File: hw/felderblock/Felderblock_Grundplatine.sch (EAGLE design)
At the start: 50 parts, among them IC1 LM311N, IC2 MC78M05CT, J1 RJ11, J2 RJ11, M1 ARDUINO-NANO-3.0, T2 BC337, X1 TASTENSPERRE1, X2 TASTENSPERRE2, X3 SCHL-SPERRE, X5 ANSCHALTER

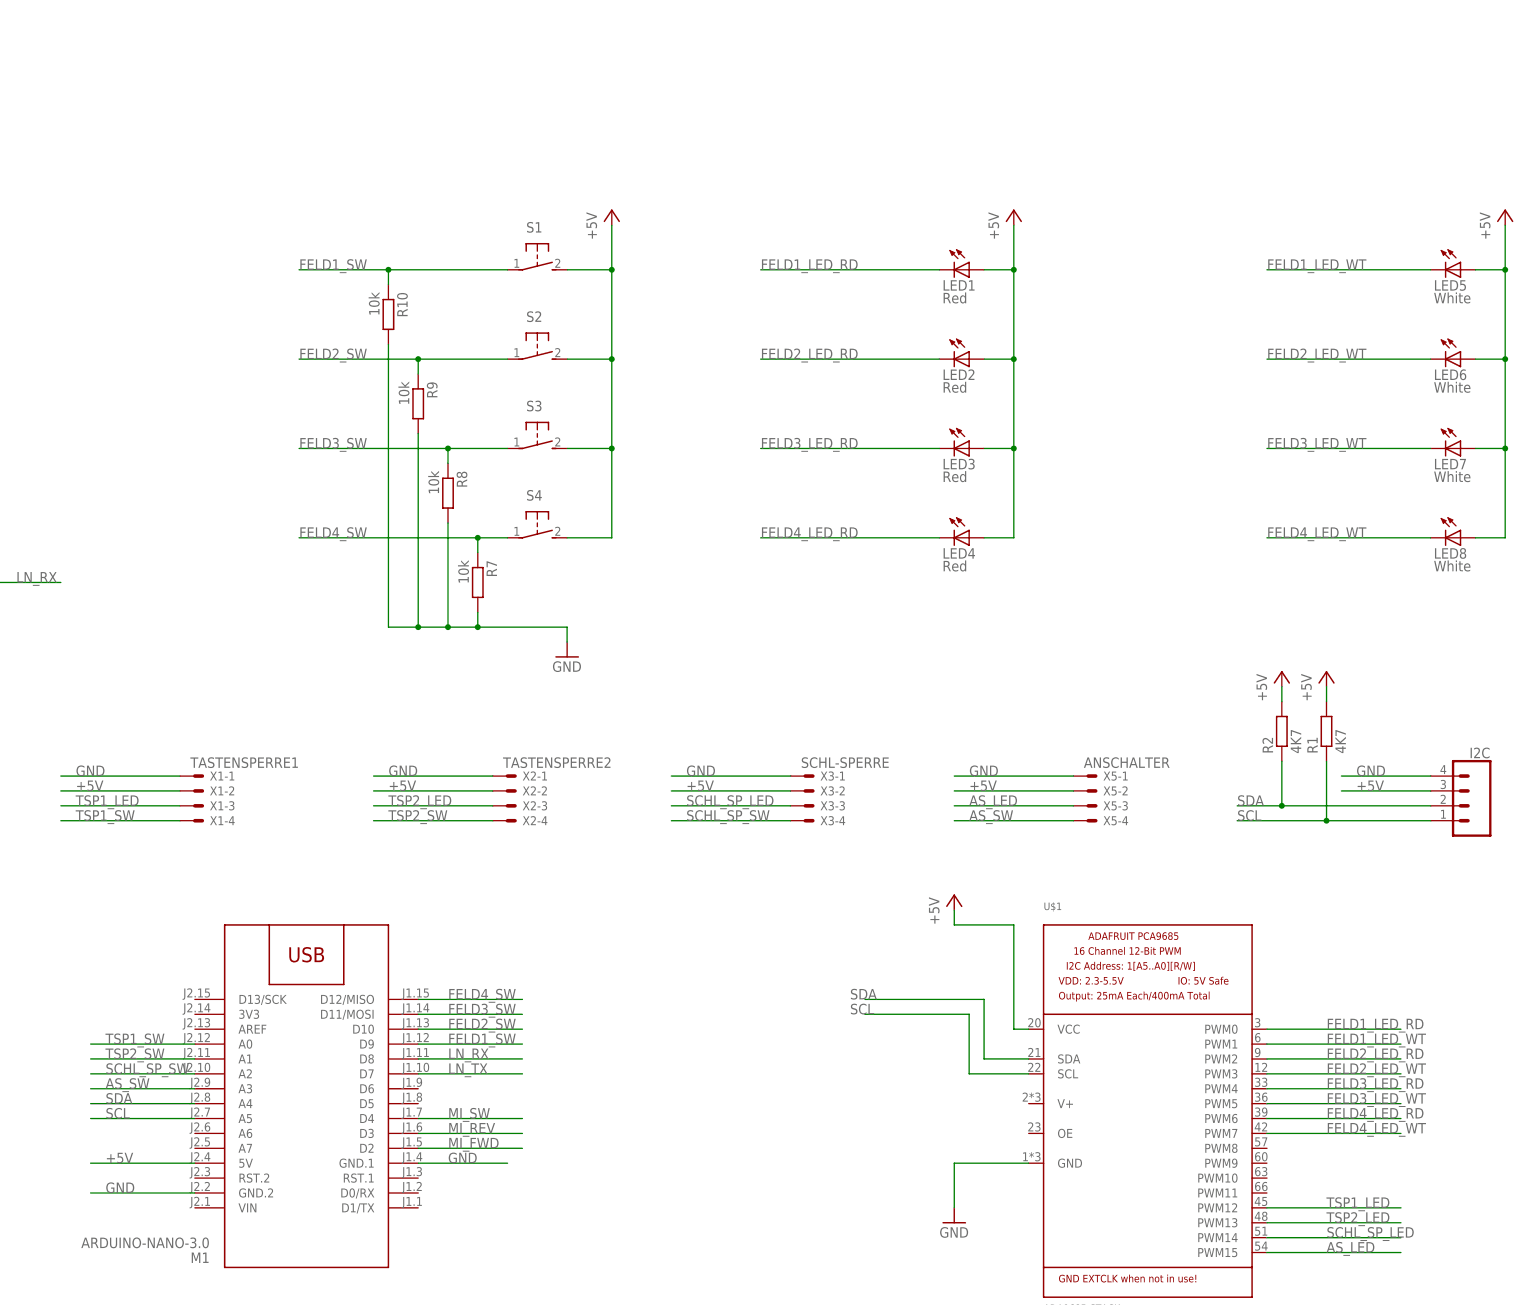
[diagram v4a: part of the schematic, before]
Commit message: Extended to six fields
Extended to six fields per PCB
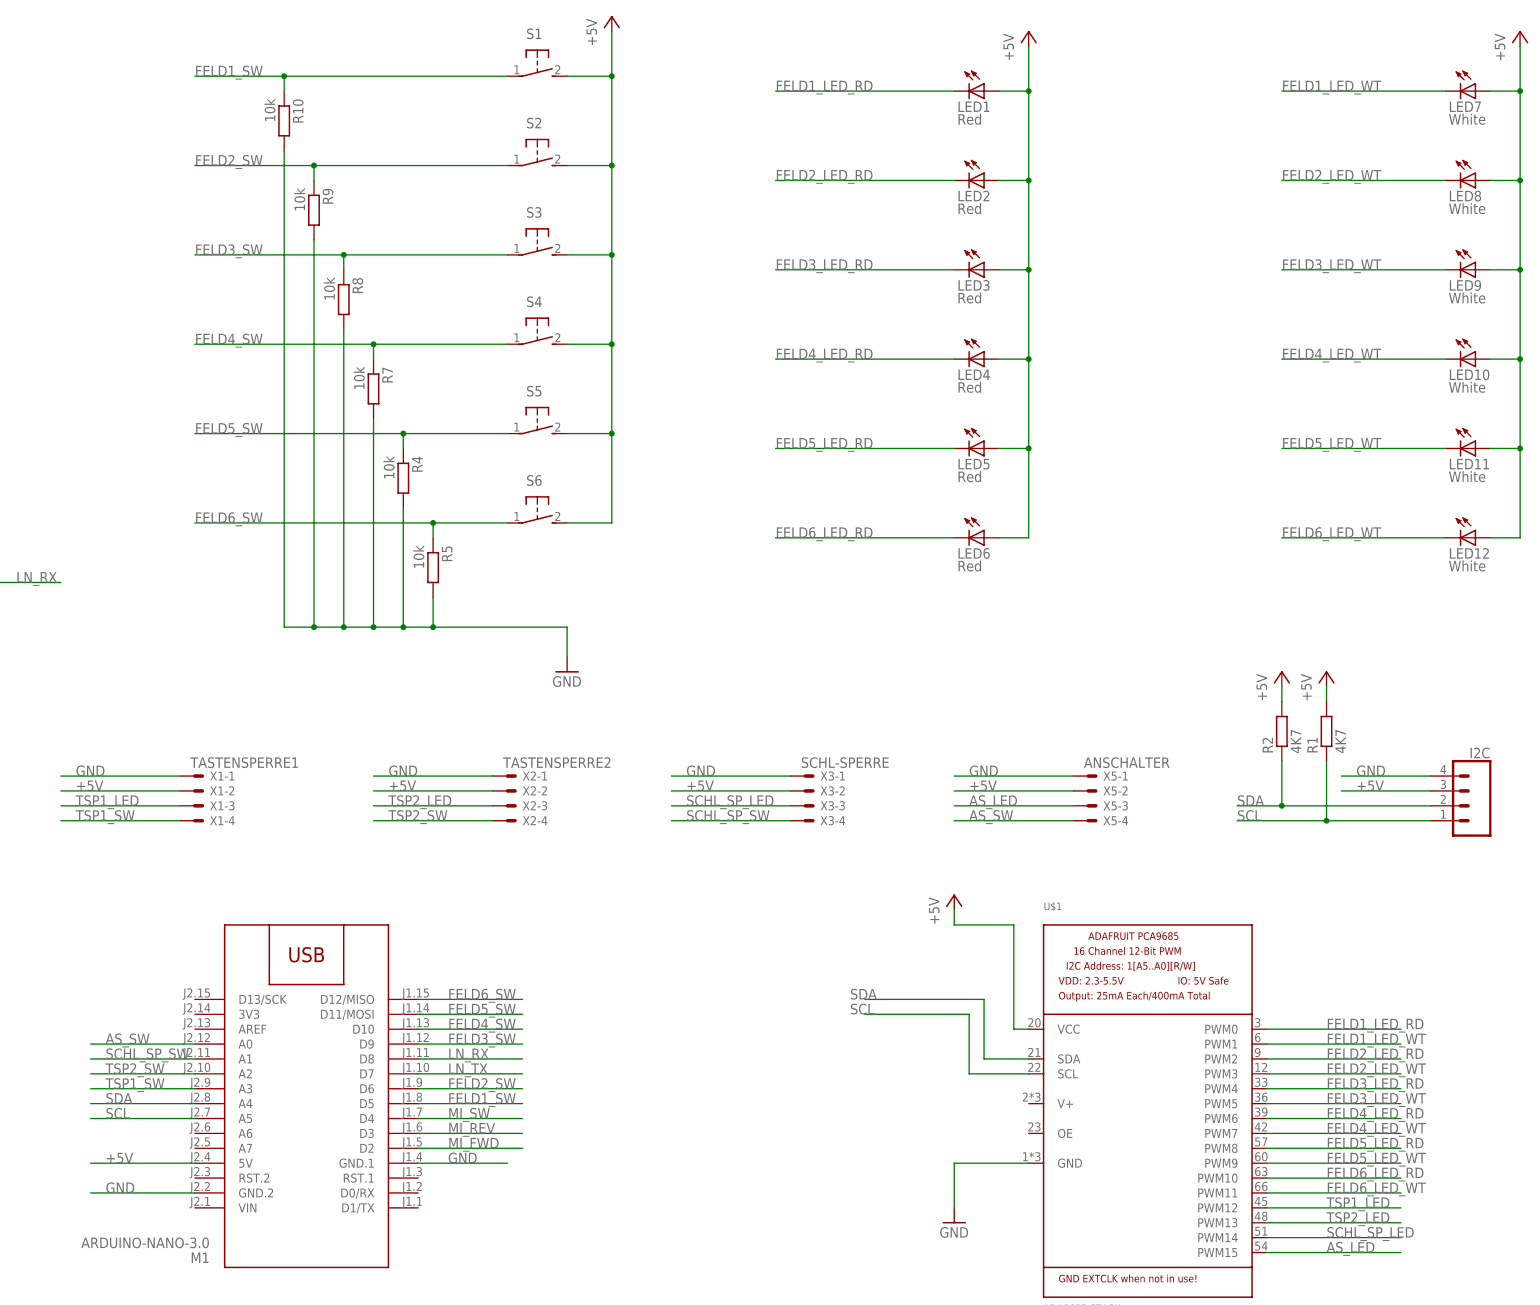
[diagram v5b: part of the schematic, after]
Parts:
- added LED10, LED11, LED12, LED9: White, led:LED3MM
- added R4, R5: 10k, resistor:R-EU_0207/7
- added S5, S6: (no value), adafruit:31-XX
- LED5, LED6: value White -> Red
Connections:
- new net FELD5_LED_RD: LED5.C, U$1.PWM8
- new net FELD5_LED_WT: LED11.C, U$1.PWM9
- new net FELD5_SW: M1.D11/MOSI, R4.1, S5.P
- new net FELD6_LED_RD: LED6.C, U$1.PWM10
- new net FELD6_LED_WT: LED12.C, U$1.PWM11
- new net FELD6_SW: M1.D12/MISO, R5.1, S6.P
- net +5V: now also LED10.A, LED11.A, LED12.A, LED9.A, S5.S, S6.S
- net AS_SW: now also M1.A0; no longer M1.A3
- net FELD1_LED_WT: now also LED7.C; no longer LED5.C
- net FELD1_SW: now also M1.D5; no longer M1.D9
- net FELD2_LED_WT: now also LED8.C; no longer LED6.C
- net FELD2_SW: now also M1.D6; no longer M1.D10
- net FELD3_LED_WT: now also LED9.C; no longer LED7.C
- net FELD3_SW: now also M1.D9; no longer M1.D11/MOSI
- net FELD4_LED_WT: now also LED10.C; no longer LED8.C
- net FELD4_SW: now also M1.D10; no longer M1.D12/MISO
- net GND: now also R4.2, R5.2
- net SCHL_SP_SW: now also M1.A1; no longer M1.A2
- net TSP1_SW: now also M1.A3; no longer M1.A0
- net TSP2_SW: now also M1.A2; no longer M1.A1
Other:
- moved on the sheet: LED1, LED2, LED3, LED4, LED5, LED6, LED7, LED8, R10, R7, R8, R9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
